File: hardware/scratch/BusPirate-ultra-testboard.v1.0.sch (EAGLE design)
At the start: 20 parts, among them J1 CON_HEADER_1X10-RIGHT_ANGLED_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

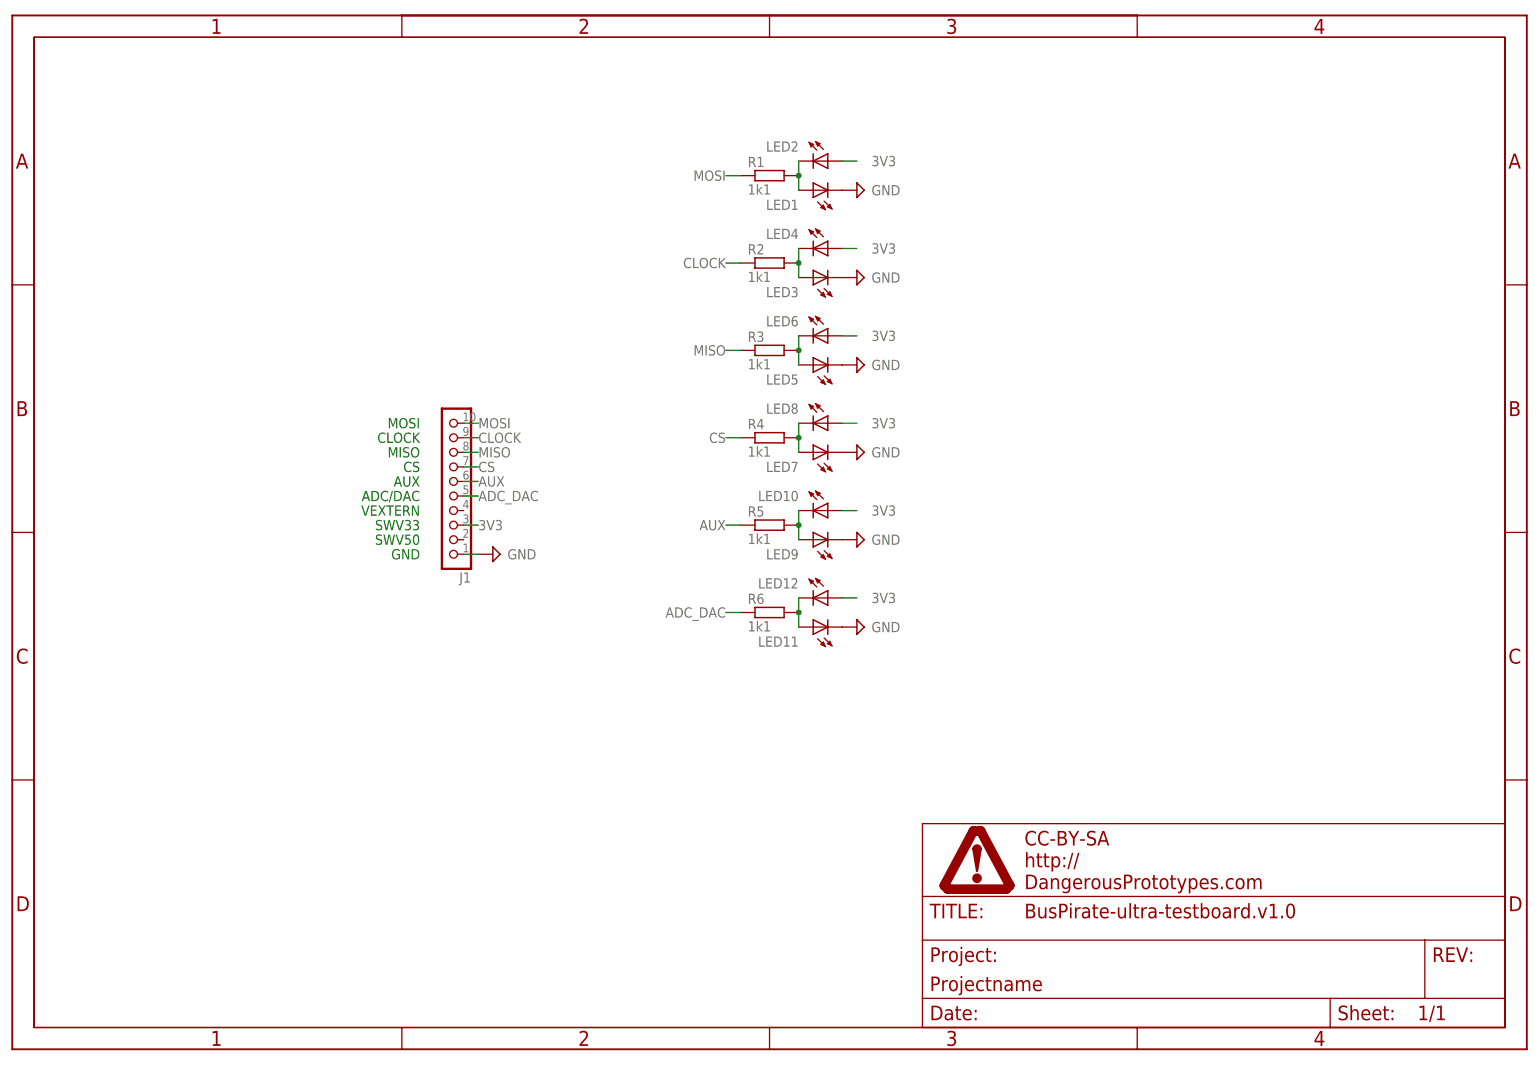
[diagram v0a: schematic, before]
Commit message: updated BP test board board, added LEDs for 5V and 3.3V
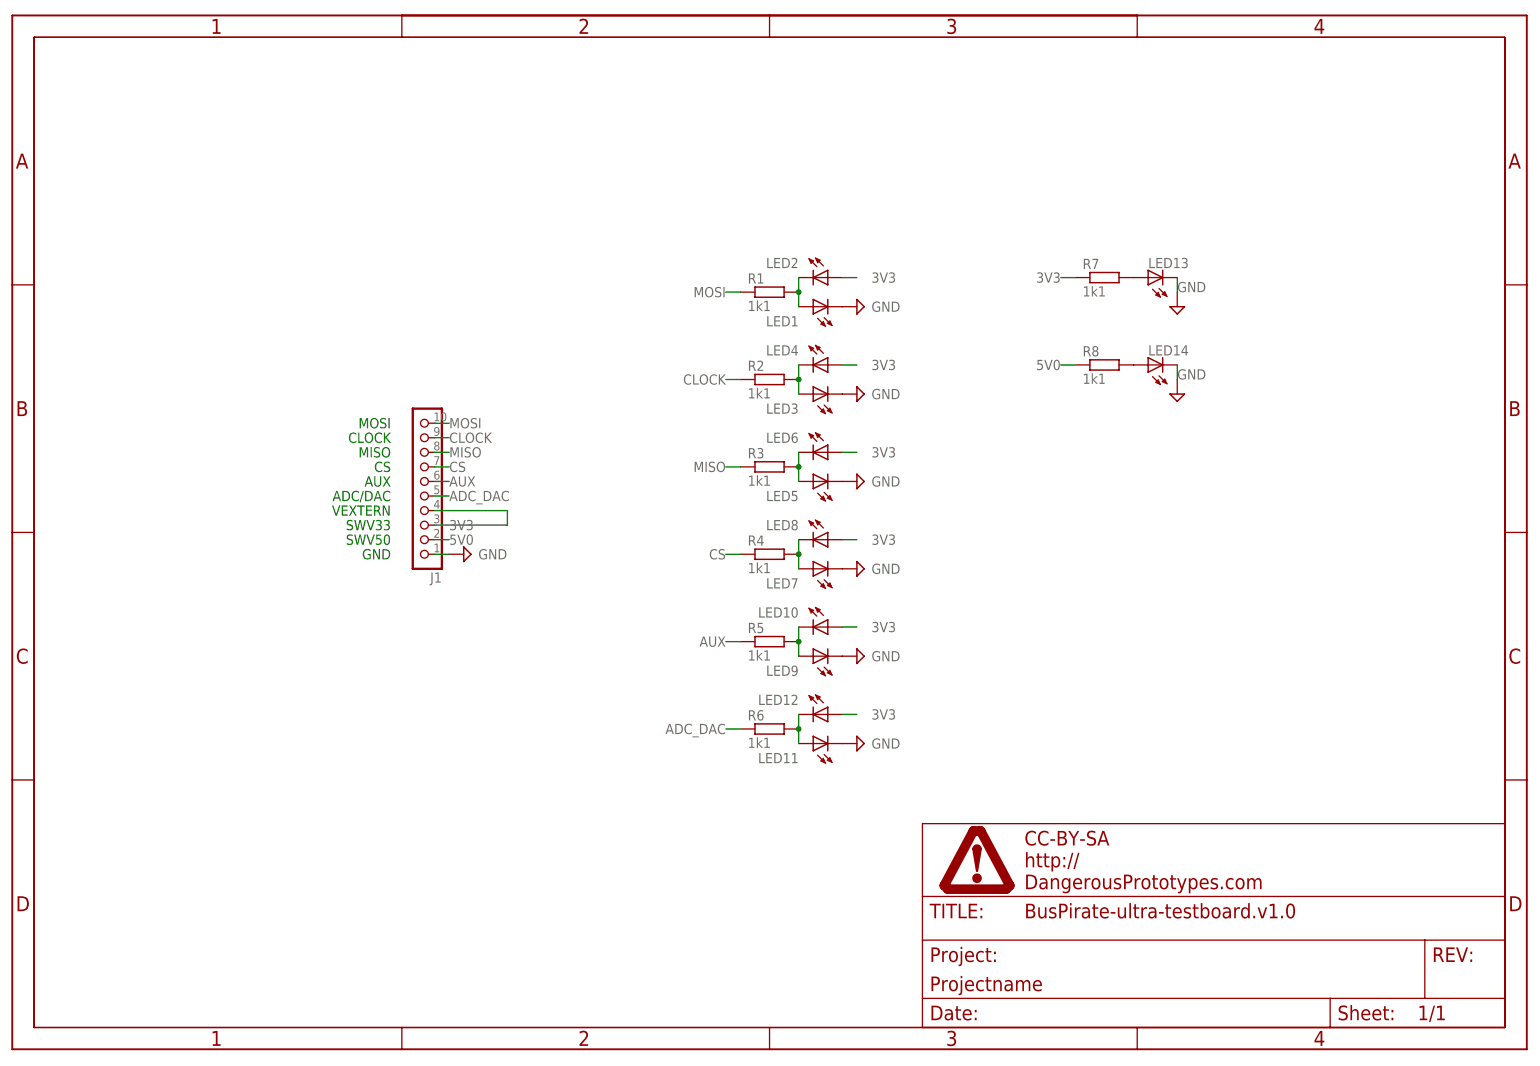
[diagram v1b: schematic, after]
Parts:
- added LED13, LED14: (no value), dp_devices.v6:LED-0805
- added R7, R8: 1k1, dp_devices.v6:RESISTOR-0603
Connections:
- new net 5V0: J1.2, R8.1
- new net N$7: LED14.A, R8.2
- new net N$8: LED13.A, R7.2
- net 3V3: now also J1.4, R7.1
- net GND: now also LED13.C, LED14.C
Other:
- moved on the sheet: J1, LED1, LED10, LED11, LED12, LED2, LED3, LED4, LED5, LED6, LED7, LED8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
